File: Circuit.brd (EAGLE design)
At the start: 99 x 72.1 mm, 114 parts, among them IC1 LM1117T-3.3-V

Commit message: Halfway
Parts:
- moved R1 38.5 mm to (73.4, 49.0), turned to 270 degrees
- moved MUX1 37.6 mm to (69.0, 49.0), turned to 180 degrees
- moved R5 5.26 mm to (44.2, 50.0), turned to 180 degrees
- moved R8 3.20 mm to (66.3, 41.4), turned to 90 degrees
- moved C3 2.16 mm to (37.0, 48.0)
- moved C1 1.72 mm to (40.0, 48.0), turned to 180 degrees
- moved R3 1.71 mm to (43.0, 48.0), turned to 0 degrees
- moved C8 1.50 mm to (54.1, 45.6), turned to 180 degrees
- moved C11 1.00 mm to (53.6, 43.6), turned to 0 degrees
- moved C6 0.72 mm to (31.0, 34.0)
- moved C18 0.60 mm to (57.6, 44.4)
- moved C5 0.20 mm to (60.0, 44.6)
- moved C9 0.20 mm to (62.0, 44.6)
- moved R10 0.20 mm to (63.4, 41.0)
- turned R7 to 180 degrees
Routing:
- net +3V3: track 153.3 -> 217.7 mm, vias 1 -> 3
- net B1_SD0: track 24.8 -> 76.0 mm, vias 2 -> 3
- net B1_SD2: track 9.50 -> 51.4 mm, vias 0 -> 4
- net B1_SC2: track 8.17 -> 49.7 mm, vias 0 -> 2
- net B1_SD1: track 2.86 -> 42.7 mm, vias 0 -> 2
- net B1_SC0: track 27.4 -> 65.2 mm, vias 0 -> 2
- net B1_SC1: track 7.71 -> 41.2 mm
- net N$8: track 9.00 -> 0.00 mm
- net N$4: track 7.00 -> 0.00 mm
- net N$42: track 0.00 -> 6.74 mm
- net GND: track 0.00 -> 3.30 mm
- net N$27: track 9.49 -> 6.58 mm
- net N$52: track 2.46 -> 4.83 mm
- net N$53: track 5.57 -> 7.72 mm
- net N$2: track 4.54 -> 3.18 mm

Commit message: <paranoia>COMMIT!</paranoia>
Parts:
- moved C33 82.0 mm to (94.0, 54.0), turned to 90 degrees
- moved C43 81.7 mm to (92.0, 60.0), flipped to the top
- moved R23 73.2 mm to (85.0, 56.0)
- moved U$3 68.4 mm to (6.66, 48.8), turned to 90 degrees
- moved R28 63.8 mm to (85.0, 54.0)
- moved R39 53.0 mm to (76.9, 75.2)
- moved C14 53.0 mm to (46.0, 74.0)
- moved C2 53.0 mm to (60.0, 74.0)
- moved C21 53.0 mm to (71.0, 68.0)
- moved C23 53.0 mm to (40.0, 76.0)
- moved C24 53.0 mm to (71.0, 64.0)
- moved C34 53.0 mm to (36.0, 57.0)
- moved C37 53.0 mm to (41.0, 57.0)
- moved C4 53.0 mm to (61.0, 57.0)
- moved C40 53.0 mm to (30.0, 74.0)
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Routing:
- net +3V3: track 217.7 -> 386.0 mm
- net B2_SD1: track 0.00 -> 79.6 mm, vias 0 -> 3
- net B2_SC1: track 0.00 -> 77.5 mm
- net B2_SD2: track 0.00 -> 73.4 mm, vias 0 -> 4
- net B2_SC2: track 0.00 -> 69.1 mm, vias 0 -> 2
- net N$7: track 0.00 -> 59.3 mm
- net N$6: track 0.00 -> 55.5 mm
- net N$35: track 0.00 -> 19.3 mm, vias 0 -> 2
- net N$45: track 0.00 -> 9.82 mm
- net N$50: track 0.00 -> 9.13 mm
- net N$46: track 0.00 -> 7.54 mm
- net CLK1: track 0.00 -> 7.51 mm
- net SDA1: track 0.00 -> 6.65 mm
- net N$34: track 0.00 -> 5.29 mm
- net N$36: track 26.3 -> 22.2 mm
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
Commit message: About to find a load of problems. Ignorance is bliss.
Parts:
- moved R28 70.8 mm to (16.0, 38.0), turned to 270 degrees
- moved C33 70.7 mm to (29.5, 25.1), turned to 270 degrees
- moved MAG2 69.1 mm to (10.0, 55.0)
- moved R23 69.1 mm to (16.0, 60.0)
- moved R40 62.6 mm to (20.9, 58.6)
- moved R39 62.6 mm to (15.9, 61.1)
- moved C43 58.0 mm to (43.5, 28.2)
- moved C24 52.0 mm to (19.0, 66.0)
- moved C4 52.0 mm to (9.00, 59.0)
- moved R4 52.0 mm to (10.0, 65.0)
- moved C2 47.9 mm to (13.0, 65.0)
- moved C21 47.9 mm to (24.0, 59.0)
- moved C46 47.9 mm to (18.0, 65.0)
- moved C49 47.9 mm to (18.0, 61.0)
- moved R6 47.9 mm to (13.0, 61.0)
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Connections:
- removed net N$11: R15.1
- removed net N$12: R18.1
- removed net N$18: R31.1
- removed net N$19: R34.1
- net I1_AUXCLK: now also R15.1
- net I1_AUXSDA: now also R18.1
- net I2_AUXCLK: now also R31.1
- net I2_AUXSDA: now also R34.1
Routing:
- net N$7: track 59.3 -> 5.94 mm
- net B2_SC0: track 0.00 -> 50.8 mm, vias 0 -> 2
- net B2_SD0: track 0.00 -> 41.4 mm, vias 0 -> 2
- net +3V3: track 386.0 -> 423.7 mm, vias 3 -> 5
- net N$6: track 55.5 -> 18.0 mm, vias 0 -> 2
- net I2_AUXCLK: track 0.00 -> 22.4 mm
- net B2_SD1: track 79.6 -> 94.0 mm, vias 3 -> 4
- net B2_SC1: track 77.5 -> 88.2 mm
- net I2_AUXSDA: track 0.00 -> 5.75 mm
- net N$20: track 0.00 -> 5.30 mm
- net N$21: track 0.00 -> 4.92 mm
- net B2_SC2: track 69.1 -> 73.0 mm
- net N$30: track 0.00 -> 2.99 mm
- net N$15: track 0.00 -> 2.94 mm
- net N$46: track 7.54 -> 4.63 mm
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
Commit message: Magnometer left
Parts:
- moved MAG2 97.8 mm to (94.0, 5.00), flipped to the top
- moved R4 97.6 mm to (92.0, 12.0)
- moved C4 97.3 mm to (90.0, 5.00), turned to 90 degrees
- moved R6 95.7 mm to (94.0, 10.0), turned to 180 degrees
- moved C2 93.8 mm to (89.0, 10.0)
- moved R16 66.6 mm to (58.8, 8.60), flipped to the top, turned to 270 degrees
- moved R19 54.4 mm to (49.8, 15.3), flipped to the top, turned to 270 degrees
- moved R2 40.3 mm to (19.0, 27.7), flipped to the top
- moved R40 37.8 mm to (19.0, 20.9)
- moved R23 36.9 mm to (19.0, 23.2)
- moved R39 35.8 mm to (19.0, 25.4)
- moved C23 33.9 mm to (19.0, 32.1), turned to 0 degrees
- moved C53 30.3 mm to (24.4, 35.5), turned to 0 degrees
- moved C14 28.1 mm to (19.0, 36.5), turned to 0 degrees
- moved C24 27.3 mm to (19.0, 38.7), flipped to the top
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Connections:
- removed net N$22: ITG4.13
- removed net N$24: C41.1
- removed net N$25: R16.1
- removed net N$26: R19.1
- net +3V3: now also C41.1, ITG4.13
- net I3_AUXCLK: now also R16.1
- net I3_AUXSDA: now also R19.1
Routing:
- net +3V3: track 423.7 -> 472.5 mm
- net M2_AUXCLK: track 0.00 -> 12.3 mm
- net M2_AUXSDA: track 0.00 -> 10.2 mm
- net N$16: track 0.00 -> 9.78 mm, vias 0 -> 2
- net B2_SC0: track 50.8 -> 57.7 mm
- net I3_AUXCLK: track 7.84 -> 14.4 mm, vias 0 -> 2
- net N$5: track 0.00 -> 4.07 mm
- net B2_SD1: track 94.0 -> 91.3 mm
- net N$14: track 7.23 -> 9.79 mm
- net B2_SC1: track 88.2 -> 86.5 mm
- net N$39: track 5.87 -> 4.57 mm
- net I3_AUXSDA: track 13.5 -> 14.4 mm
- net B1_SD0: track 76.0 -> 76.7 mm

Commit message: Fixing a few schematic errors
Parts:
- moved R4 16.2 mm to (86.0, 27.0)
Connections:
- removed net N$32: R32.1
- removed net N$33: R35.1
- removed net SCL2: R40.1, U$3.P5_4
- net CLK2: now also R40.1, U$3.P5_4
- net I4_AUXCLK: now also R32.1
- net I4_AUXSDA: now also R35.1
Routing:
- net M2_AUXCLK: track 12.3 -> 26.5 mm
- net M2_AUXSDA: track 10.2 -> 17.6 mm
- net B2_SD0: vias 2 -> 4
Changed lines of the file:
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@@
 <element name="C2" library="SparkFun" package="0603-CAP" value="0.1uF" x="89" y="10" rot="R180"/>
 <element name="C4" library="SparkFun" package="0603-CAP" value="0.1uF" x="90" y="5" rot="R90"/>
-<element name="R4" library="resistor" package="R0603" value="2.2K" x="92" y="12"/>
+<element name="R4" library="resistor" package="R0603" value="2.2K" x="86" y="27"/>
 <element name="R6" library="resistor" package="R0603" value="2.2K" x="94" y="10" rot="R180"/>
 <element name="MUX1" library="Gyros" package="TSSOP16" value="PCA9546A" x="74" y="24" smashed="yes" rot="R180">
@@
 <wire x1="19.83" y1="25.45" x2="2.85" y2="56.45" width="0" layer="19" extent="1-1"/>
 <wire x1="25.625" y1="23.0822" x2="19.83" y2="25.45" width="0" layer="19" extent="1-1"/>
-</signal>
-<signal name="SCL2">
-<contactref element="U$3" pad="P5_4"/>
-<contactref element="R40" pad="1"/>
-<wire x1="19.85" y1="20.9" x2="5.39" y2="56.45" width="0" layer="19" extent="1-1"/>
 </signal>
 <signal name="N$3">
@@
 <wire x1="18.15" y1="20.9" x2="18.1" y2="20.9" width="0.254" layer="1"/>
 <wire x1="18.1" y1="20.9" x2="18" y2="21" width="0.254" layer="1"/>
-<wire x1="77" y1="39" x2="77" y2="38.85" width="0" layer="19" extent="1-1"/>
+<wire x1="81" y1="28" x2="86.85" y2="27" width="0" layer="19" extent="1-1"/>
+<wire x1="77" y1="38.85" x2="77" y2="39" width="0" layer="19" extent="1-1"/>
 <wire x1="51.725" y1="35" x2="53.5" y2="35.275" width="0" layer="19" extent="1-1"/>
 <wire x1="24.6" y1="39.85" x2="22.3" y2="39.85" width="0" layer="19" extent="1-1"/>
@@
 <wire x1="32.6379" y1="25.8784" x2="33.1425" y2="25.8784" width="0" layer="19" extent="1-1"/>
 <wire x1="7.25" y1="7.35" x2="20" y2="7.7" width="0" layer="19" extent="1-1"/>
-<wire x1="92.85" y1="12" x2="78" y2="10.85" width="0" layer="19" extent="1-1"/>
-<wire x1="93.15" y1="10" x2="92.85" y2="12" width="0" layer="19" extent="1-1"/>
+<wire x1="93.15" y1="10" x2="78" y2="10.85" width="0" layer="19" extent="1-1"/>
 <wire x1="93.09" y1="5.4" x2="93.15" y2="10" width="0" layer="19" extent="1-1"/>
 <wire x1="94.91" y1="5" x2="93.09" y2="5.4" width="0" layer="19" extent="1-1"/>
@@
 <wire x1="22" y1="36" x2="22" y2="35" width="0.254" layer="1"/>
 <wire x1="22" y1="35" x2="23.4" y2="33.6" width="0.254" layer="1"/>
-<wire x1="23.4" y1="33.6" x2="26.625" y2="33.6" width="0.254" layer="1"/>
-<wire x1="26.725" y1="33.5" x2="32.1333" y2="25.8784" width="0" layer="19" extent="1-1"/>
+<wire x1="23.4" y1="33.6" x2="24" y2="33.6" width="0.254" layer="1"/>
+<wire x1="24" y1="33.6" x2="26.625" y2="33.6" width="0.254" layer="1"/>
+<wire x1="32.1333" y1="25.8784" x2="32.1" y2="25.8784" width="0.254" layer="1"/>
+<wire x1="32.1" y1="25.8784" x2="32.1" y2="25.6" width="0.254" layer="1"/>
+<wire x1="32.1" y1="25.6" x2="31.4" y2="25.6" width="0.254" layer="1"/>
+<wire x1="31.4" y1="25.6" x2="30" y2="27" width="0.254" layer="1"/>
+<wire x1="30" y1="27" x2="30" y2="27.5" width="0.254" layer="1"/>
+<wire x1="30" y1="27.5" x2="29" y2="28.5" width="0.254" layer="1"/>
+<wire x1="29" y1="28.5" x2="27.5" y2="28.5" width="0.254" layer="1"/>
+<wire x1="27.5" y1="28.5" x2="27" y2="29" width="0.254" layer="1"/>
+<wire x1="27" y1="29" x2="27" y2="31" width="0.254" layer="1"/>
+<wire x1="27" y1="31" x2="26" y2="32" width="0.254" layer="1"/>
+<wire x1="26" y1="32" x2="24" y2="32" width="0.254" layer="1"/>
+<wire x1="24" y1="32" x2="24" y2="33.6" width="0.254" layer="1"/>
 </signal>
 <signal name="M2_AUXSDA">
@@
 <wire x1="27.8" y1="31.5" x2="27.5" y2="31.8" width="0.254" layer="1"/>
 <wire x1="27.5" y1="31.8" x2="27.5" y2="32.725" width="0.254" layer="1"/>
-<wire x1="29.5" y1="31.5" x2="31.3338" y2="26.7033" width="0" layer="19" extent="1-1"/>
+<wire x1="31.3338" y1="26.7033" x2="30.8967" y2="26.7033" width="0.254" layer="1"/>
+<wire x1="30.8967" y1="26.7033" x2="30.6" y2="27" width="0.254" layer="1"/>
+<wire x1="30.6" y1="27" x2="30.6" y2="27.9" width="0.254" layer="1"/>
+<wire x1="30.6" y1="27.9" x2="30.5" y2="27.9" width="0.254" layer="1"/>
+<wire x1="30.5" y1="27.9" x2="29.3" y2="29.1" width="0.254" layer="1"/>
+<wire x1="29.3" y1="29.1" x2="28" y2="29.1" width="0.254" layer="1"/>
+<wire x1="28" y1="29.1" x2="27.7" y2="29.4" width="0.254" layer="1"/>
+<wire x1="27.7" y1="29.4" x2="27.7" y2="31.4" width="0.254" layer="1"/>
+<wire x1="27.7" y1="31.4" x2="27.8" y2="31.5" width="0.254" layer="1"/>
 </signal>
 <signal name="CLK2">
 <contactref element="MUX2" pad="14"/>
+<contactref element="U$3" pad="P5_4"/>
+<contactref element="R40" pad="1"/>
+<wire x1="19.85" y1="20.9" x2="5.39" y2="56.45" width="0" layer="19" extent="1-1"/>
+<wire x1="24.975" y1="23.0822" x2="19.85" y2="20.9" width="0" layer="19" extent="1-1"/>
 </signal>
 <signal name="N$9">
@@
 <wire x1="49.9" y1="33.9" x2="49.9" y2="33.05" width="0.254" layer="1"/>
 <wire x1="49.9" y1="33.05" x2="49.85" y2="33" width="0.254" layer="1"/>
-</signal>
-<signal name="N$32">
-<contactref element="R32" pad="1"/>
-</signal>
-<signal name="N$33">
-<contactref element="R35" pad="1"/>
 </signal>
 <signal name="N$34">
@@
 <contactref element="ITG4" pad="6"/>
 <contactref element="ACL_6" pad="6"/>
+<contactref element="R35" pad="1"/>
 <wire x1="52.5" y1="32.725" x2="55.9338" y2="30.7033" width="0" layer="19" extent="1-1"/>
+<wire x1="52" y1="37.15" x2="52.5" y2="32.725" width="0" layer="19" extent="1-1"/>
 </signal>
 <signal name="I4_AUXCLK">
 <contactref element="ITG4" pad="7"/>
 <contactref element="ACL_6" pad="4"/>
-<wire x1="51.725" y1="33.5" x2="56.7333" y2="29.8784" width="0" layer="19" extent="1-1"/>
+<contactref element="R32" pad="1"/>
+<wire x1="51.725" y1="33.5" x2="54" y2="37.15" width="0" layer="19" extent="1-1"/>
+<wire x1="56.7333" y1="29.8784" x2="51.725" y2="33.5" width="0" layer="19" extent="1-1"/>
 </signal>
 <signal name="N$39">
@@
 <wire x1="39.7" y1="36" x2="40" y2="36" width="0.254" layer="1"/>
 <wire x1="40" y1="36" x2="40.6" y2="36.6" width="0.254" layer="1"/>
-<wire x1="32.1333" y1="30.0816" x2="32.1333" y2="30.8667" width="0.254" layer="1"/>
-<wire x1="32.1333" y1="30.8667" x2="31.6" y2="31.4" width="0.254" layer="1"/>
-<wire x1="31.6" y1="31.4" x2="30.7" y2="31.4" width="0.254" layer="1"/>
-<wire x1="30.7" y1="31.4" x2="30.3" y2="31" width="0.254" layer="1"/>
-<wire x1="30.3" y1="31" x2="28.3" y2="26.9" width="0.254" layer="1"/>
-<wire x1="28.3" y1="26.9" x2="28.1" y2="26.7" width="0.254" layer="1"/>
+<wire x1="28.1" y1="26.7" x2="28.6" y2="27.2" width="0.254" layer="1"/>
+<via x="28.6" y="27.2" extent="1-16" drill="0.6"/>
+<wire x1="28.6" y1="27.2" x2="29.2" y2="27.2" width="0.254" layer="16"/>
+<wire x1="29.2" y1="27.2" x2="30" y2="28" width="0.254" layer="16"/>
+<wire x1="30" y1="28" x2="30" y2="30" width="0.254" layer="16"/>
+<wire x1="30" y1="30" x2="31" y2="31" width="0.254" layer="16"/>
+<via x="31" y="31" extent="1-16" drill="0.6"/>
+<wire x1="31" y1="31" x2="31.9" y2="31" width="0.254" layer="1"/>
+<wire x1="31.9" y1="31" x2="32.2" y2="30.7" width="0.254" layer="1"/>
+<wire x1="32.2" y1="30.7" x2="32.2" y2="30.1483" width="0.254" layer="1"/>
+<wire x1="32.2" y1="30.1483" x2="32.1333" y2="30.0816" width="0.254" layer="1"/>
 <wire x1="19.85" y1="23.2" x2="24.3" y2="26.7" width="0" layer="19" extent="1-1"/>
 </signal>
@@
 <wire x1="21.6" y1="23.1" x2="21.7072" y2="23.1" width="0.254" layer="1"/>
 <wire x1="21.7072" y1="23.1" x2="21.725" y2="23.0822" width="0.254" layer="1"/>
-<wire x1="94.91" y1="4.2" x2="91.15" y2="12" width="0" layer="19" extent="1-1"/>
-<wire x1="76" y1="30" x2="91.15" y2="12" width="0" layer="19" extent="1-16"/>
+<wire x1="76" y1="30" x2="85.15" y2="27" width="0" layer="19" extent="1-16"/>
+<wire x1="94.91" y1="4.2" x2="85.15" y2="27" width="0" layer="19" extent="1-1"/>
 </signal>
 <signal name="I2C_MUX_2">

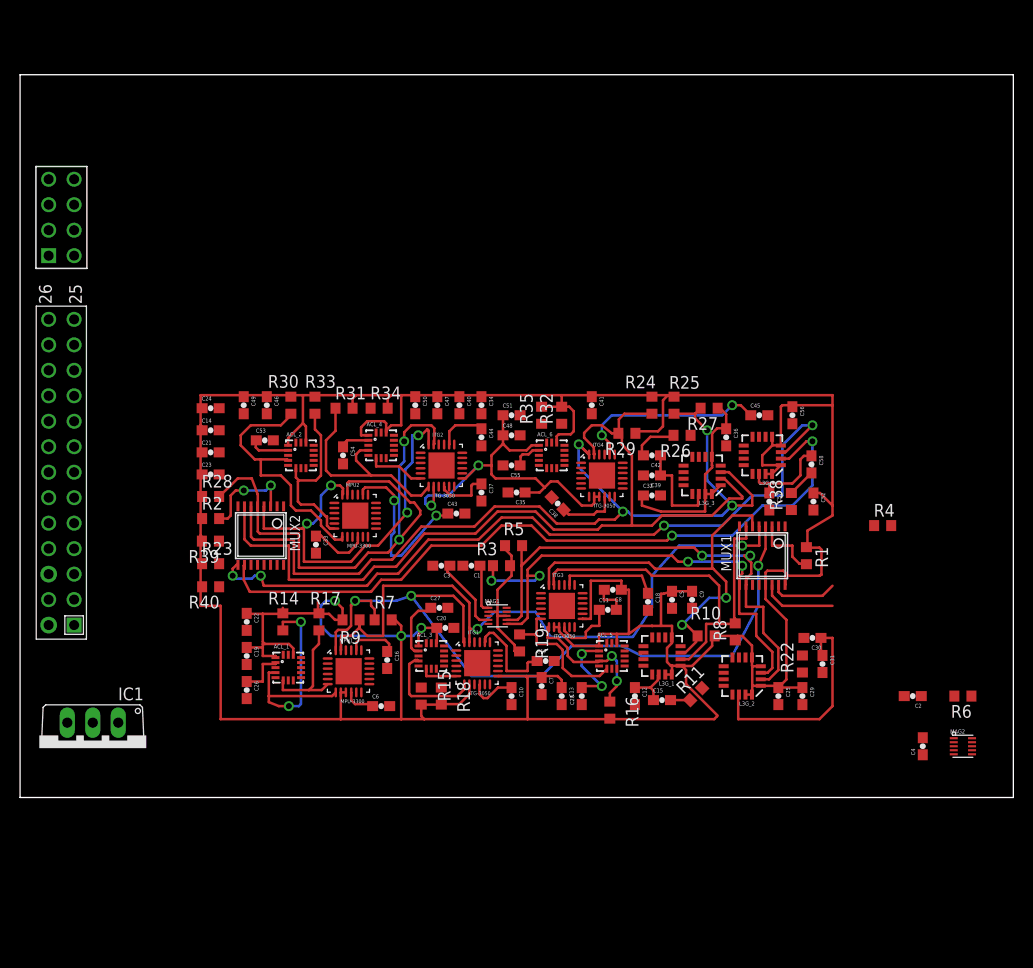
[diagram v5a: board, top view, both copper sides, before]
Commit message: Finished preliminary component positioning + routeing
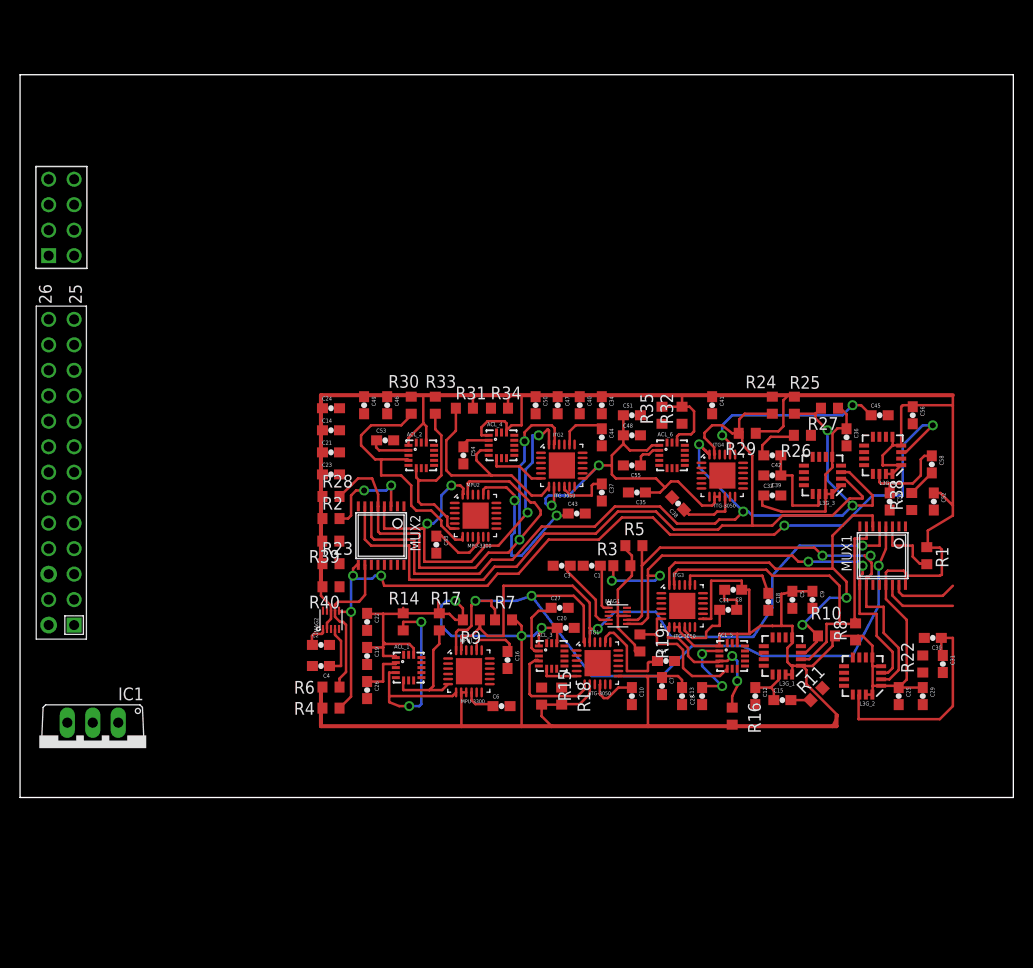
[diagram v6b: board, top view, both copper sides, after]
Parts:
- moved MAG2 64.2 mm to (31.0, 17.6), turned to 90 degrees
- moved R6 63.0 mm to (31.0, 10.9)
- moved C4 60.5 mm to (30.0, 13.0), turned to 180 degrees
- moved C2 59.2 mm to (30.0, 15.1), turned to 0 degrees
- moved R4 57.9 mm to (31.0, 8.80), turned to 180 degrees
- moved R16 12.2 mm to (71.0, 8.00)
- moved C17 12.0 mm to (64.4, 13.5)
- moved ACL_1 12.0 mm to (38.7, 12.8)
- moved R14 12.0 mm to (38.2, 17.4)
- moved ACL_2 12.0 mm to (40.0, 34.0)
- moved ACL_3 12.0 mm to (53.0, 14.0)
- moved ACL_4 12.0 mm to (48.0, 35.0)
- moved ACL_5 12.0 mm to (71.0, 14.0)
- moved ACL_6 12.0 mm to (65.0, 34.0)
- moved C1 12.0 mm to (57.0, 23.0)
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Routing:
- net +3V3: track 472.5 -> 555.6 mm
- net B2_SC2: track 73.0 -> 15.5 mm, vias 2 -> 0
- net B2_SD2: track 75.5 -> 90.6 mm, vias 4 -> 5
- net N$49: track 0.00 -> 5.09 mm
- net N$38: track 0.00 -> 2.53 mm
